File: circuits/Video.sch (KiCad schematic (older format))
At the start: 3 parts

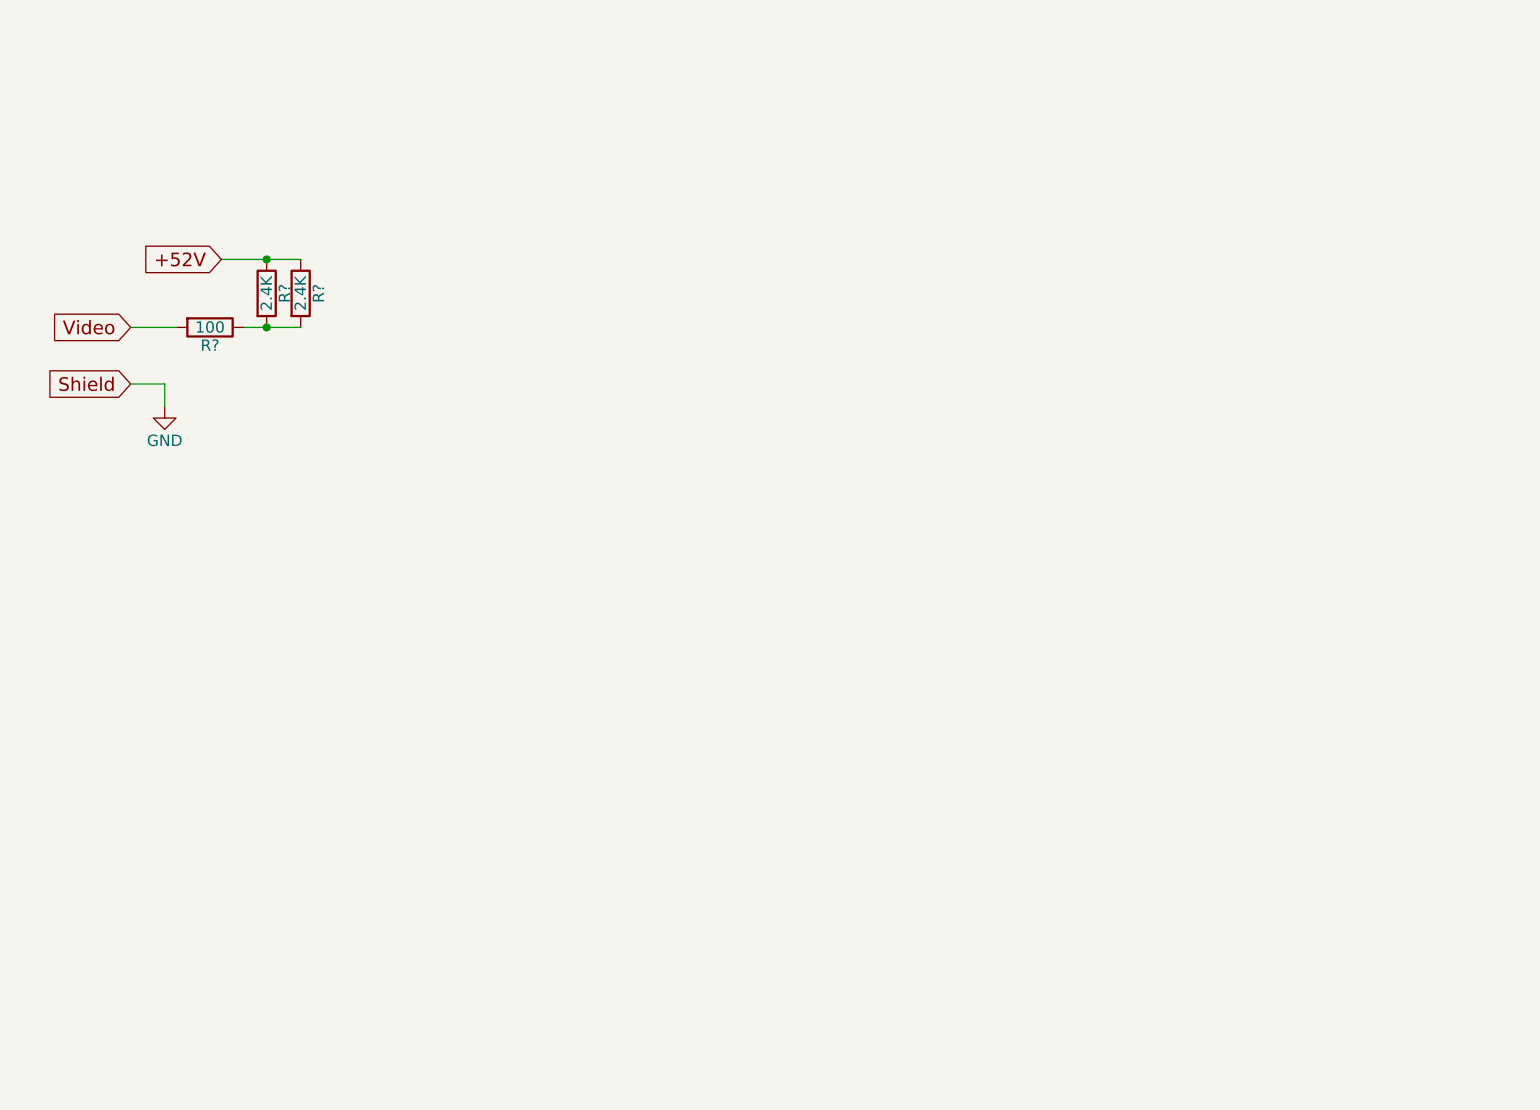
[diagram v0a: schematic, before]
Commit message: continuing to reverse video output stage
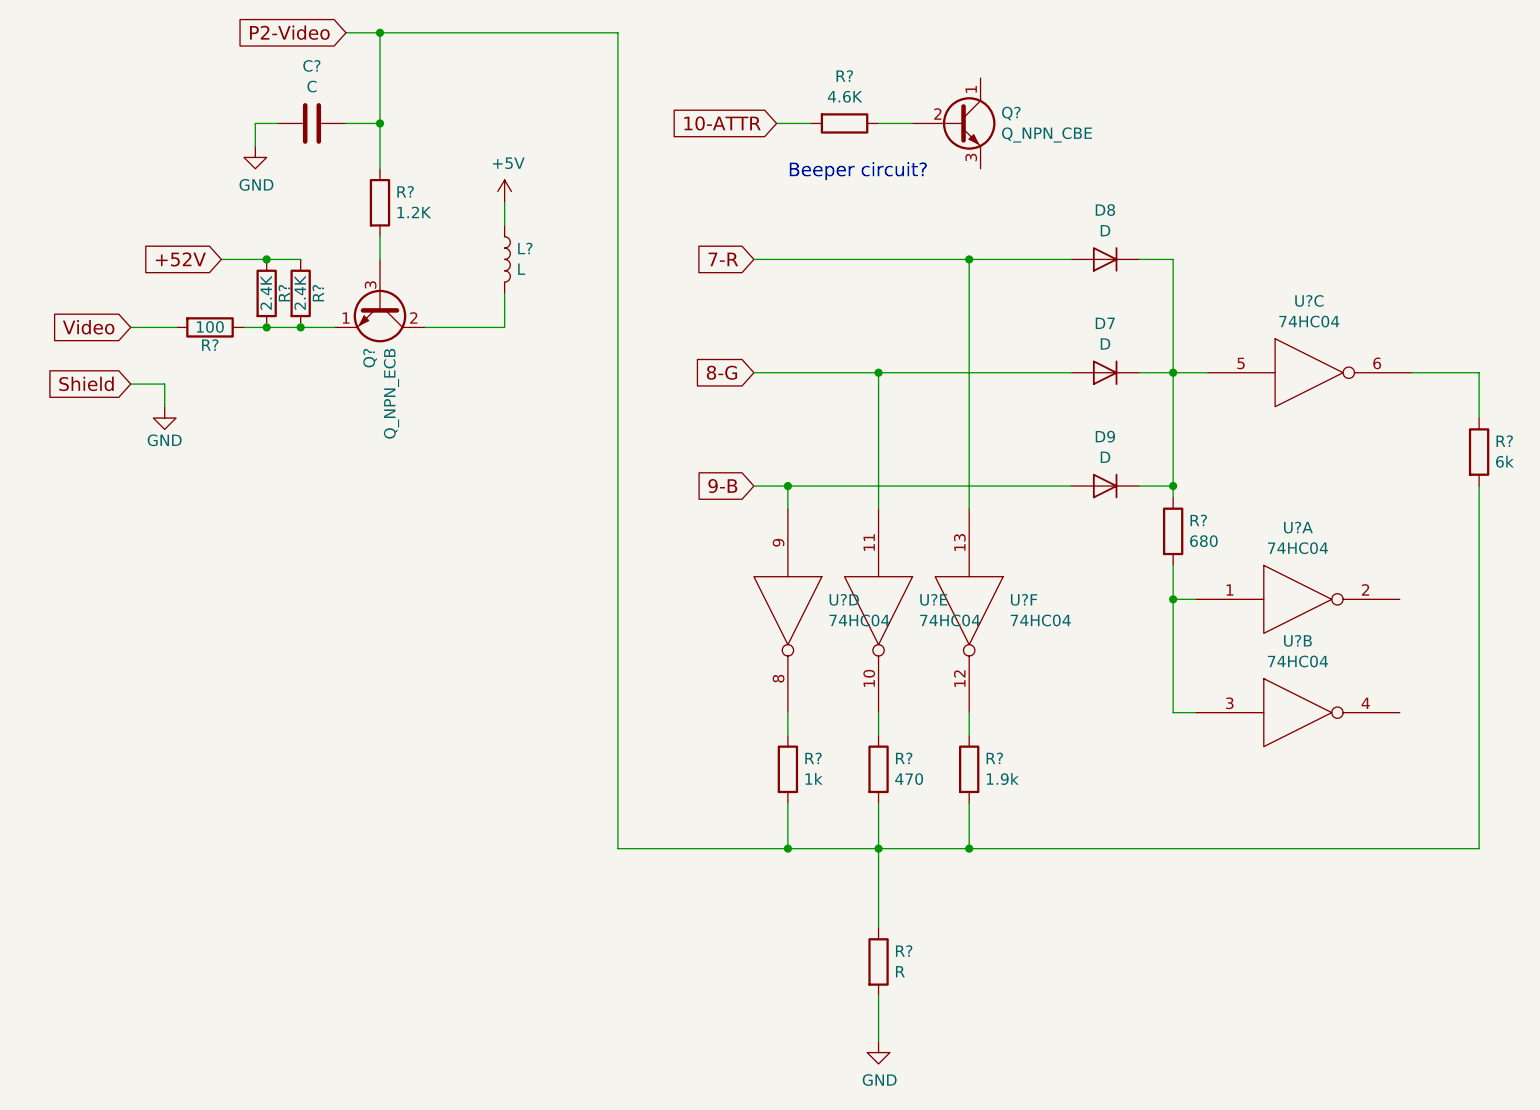
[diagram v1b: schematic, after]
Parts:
- added C?: C, symbol C
- added D7, D8, D9: D, symbol D
- added L?: L, symbol L
- added Q?: Q_NPN_ECB, symbol Q_NPN_ECB
- added Q?: Q_NPN_CBE, symbol Q_NPN_CBE
- added R?: 1.2K, symbol R
- added R?: 4.6K, symbol R
- added R?: 680, symbol R
- added R?: 1k, symbol R
- added R?: 470, symbol R
- added R?: 1.9k, symbol R
- added R?: R, symbol R
- added R?: 6k, symbol R
- added U? (x6): 74HC04, symbol 74HC04
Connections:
- net GND: now also C?.2, R?.2, U?.7 (GND), U?.7 (GND), U?.7 (GND), U?.7 (GND), U?.7 (GND), U?.7 (GND)
- net at R?.1, R?.2, R?.2: now also Q?.1 (E)
- new net: L?.2, Q?.2 (C)
- new net: Q?.3 (B), R?.2
- new net: Q?.2 (B), R?.1
- new net: D7.1 (K), D8.1 (K), D9.1 (K), R?.1, U?.5
- new net: R?.2, U?.1, U?.3
- new net: R?.1, U?.6
- new net: R?.1, U?.8
- new net: R?.1, U?.10
- new net: R?.1, U?.12
- new net +5V: L?.1
- new net 10-ATTR: R?.2
- new net 7-R: D8.2 (A), U?.13
- new net 8-G: D7.2 (A), U?.11
- new net 9-B: D9.2 (A), U?.9
- new net P2-Video: C?.1, R?.1, R?.1, R?.2, R?.2, R?.2, R?.2
- new net VCC: U?.14 (VCC), U?.14 (VCC), U?.14 (VCC), U?.14 (VCC), U?.14 (VCC), U?.14 (VCC)
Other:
- note added: "Beeper circuit?"
